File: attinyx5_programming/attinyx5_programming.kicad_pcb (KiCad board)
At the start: 2 copper layers, 19.2 x 20 mm, 6 parts, among them P2 CONN_01X06, U1 ATTINY85-20SU, Y1 Crystal

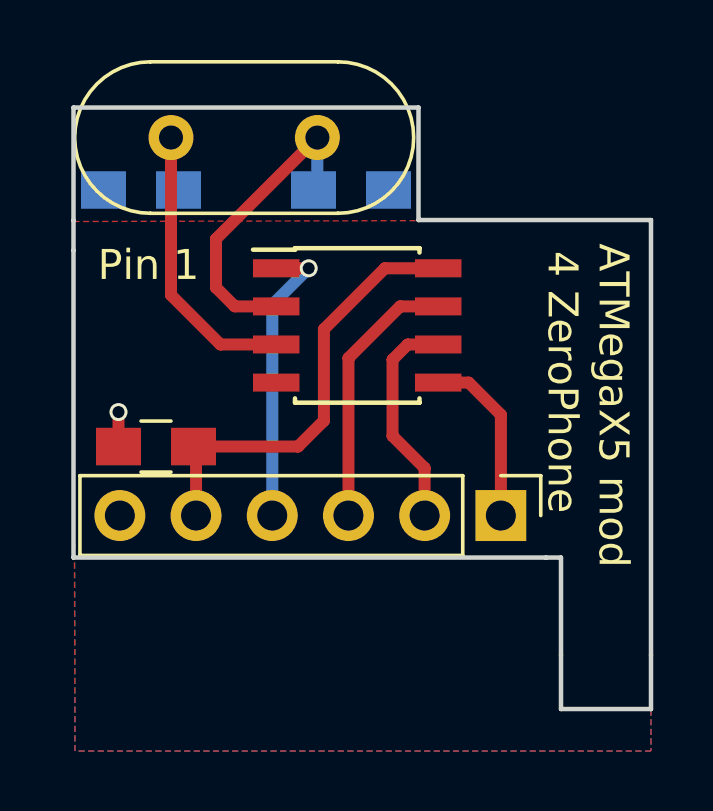
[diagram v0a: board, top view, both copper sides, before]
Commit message: v1.1 of ATTiny PCB - fixing the ATTiny FP, adding an additional ATTIny to track the RST pin
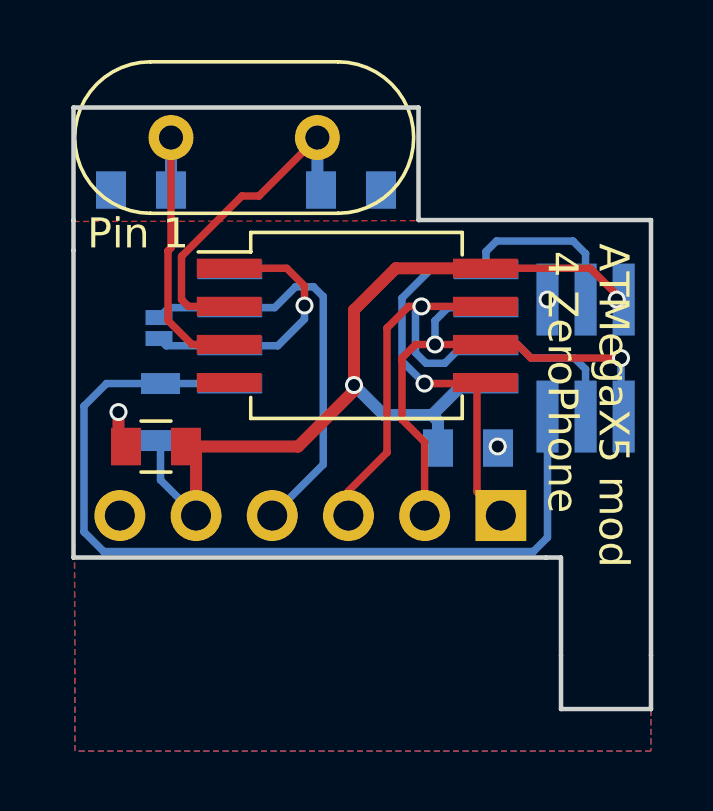
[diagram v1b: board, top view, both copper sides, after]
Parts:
- added C4: C_Small, Capacitors_SMD:C_0805, B.Cu at (153.9, 108.1)
- added CON1: AVR-ISP-6, Pin_Headers:Pin_Header_Straight_2x03_Pitch1.27mm_SMD, B.Cu at (157.8, 105.1)
- added JP1: Jumper, footprints:GS2_SMALL, B.Cu at (143.6, 103.8)
- added R1: 10K, Resistors_SMD:R_0805, B.Cu at (143.7, 106.9)
- added U2: ATTINY13-20SU, Housings_SOIC:SSO-8_6.8x5.9mm_Pitch1.27mm_Clearance7mm, B.Cu at (150.2, 104.1)
- C1, C2, C3: footprint Capacitors_SMD:C_0805_HandSoldering -> Capacitors_SMD:C_0805
- P2: moved to B.Cu
- U1: footprint Housings_SOIC:SOIC-8_3.9x4.9mm_Pitch1.27mm -> Housings_SOIC:SSO-8_6.8x5.9mm_Pitch1.27mm_Clearance7mm
- turned P2 to 90 degrees
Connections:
- U1 pad 1: CS -> RST
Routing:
- net Net-(CON1-Pad5): track 0.00 -> 29.3 mm
- net +3V3: track 14.6 -> 30.5 mm, vias 0 -> 2
- net MOSI: track 5.96 -> 19.1 mm, vias 0 -> 1
- net CLK: track 8.96 -> 20.6 mm, vias 0 -> 1
- net MISO: track 7.37 -> 17.9 mm, vias 0 -> 2
- net RST: track 0.00 -> 9.18 mm, vias 0 -> 1
- net CS: track 9.83 -> 14.0 mm, vias 1 -> 0
- net Net-(C3-Pad1): track 11.3 -> 10.4 mm
- net Net-(C2-Pad2): track 10.5 -> 11.1 mm
- net GND: track 1.30 -> 1.47 mm, vias 1 -> 3
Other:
- board text added: "G O V"
- board text added: "R K I"
- board text added: "v1.2"
- board text removed: "1"
- board text removed: "cs vcc x1 clk x2 miso gnd mosi"
- board text removed: "v1.1"
